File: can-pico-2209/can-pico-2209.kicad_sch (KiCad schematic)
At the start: 13 parts, among them J1 MERG 12v CBUS, J2 Adafruit CAN Pal, J3 DEBUG, J4 UART0, J5 Pico LHS, J6 Pico RHS, SW1 RESET, U1 LM7805_TO220

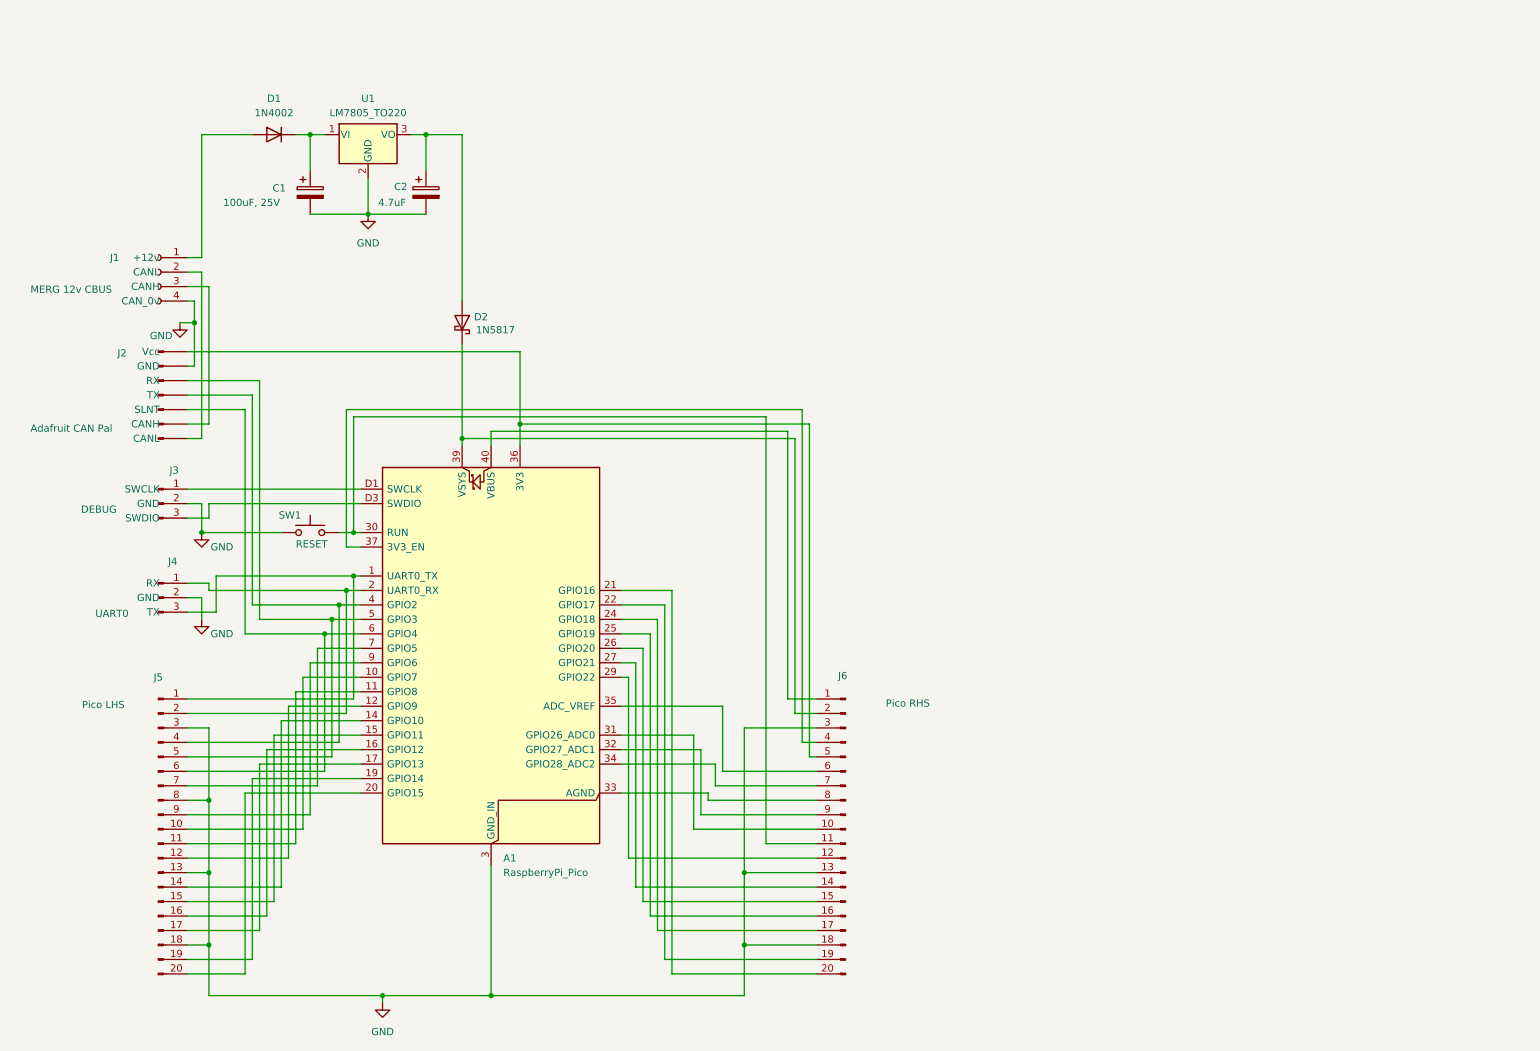
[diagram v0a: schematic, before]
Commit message: now has 2209 module wired in
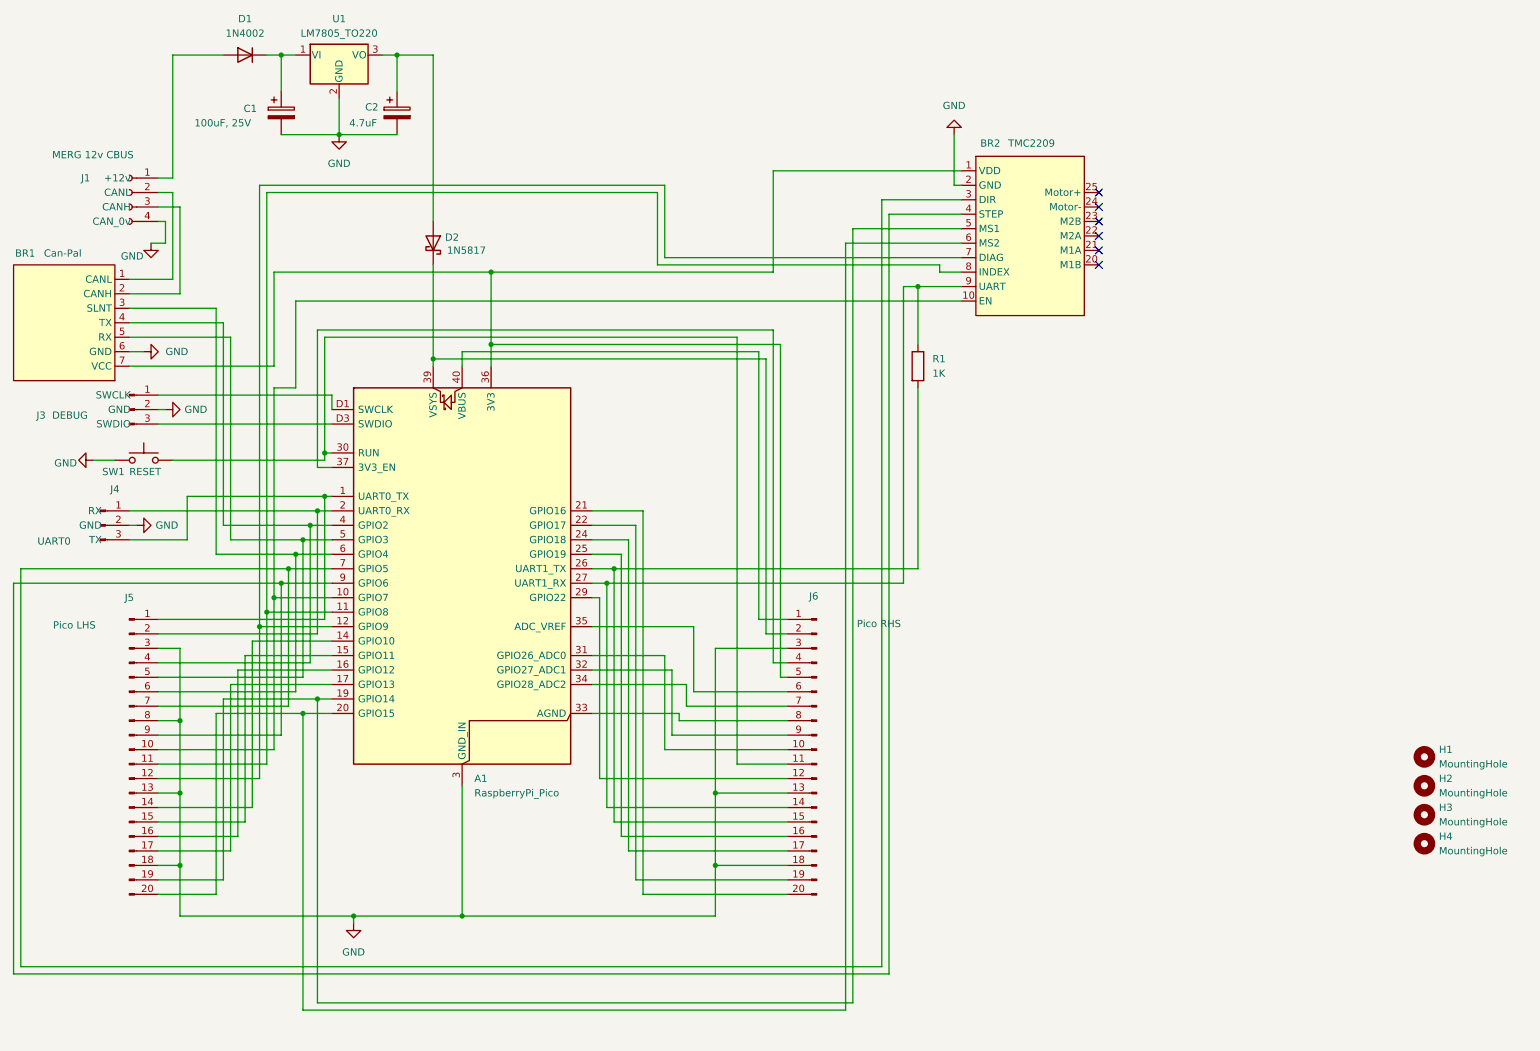
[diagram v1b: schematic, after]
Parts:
- removed J2: Adafruit CAN Pal, Connector_PinHeader_2.54mm:PinHeader_1x07_P2.54mm_Vertical, symbol Connector:Conn_01x07_Pin
- added BR1: Can-Pal, Adafruit:CAN-Pal, symbol Adafruit:CAN-Pal
- added BR2: TMC2209, Adafruit:Adafruit 2209, symbol Adafruit:TMC2209
- added H1, H2, H3, H4: MountingHole, MountingHole:MountingHole_3.2mm_M3, symbol Mechanical:MountingHole
- added R1: 1K, Resistor_THT:R_Axial_DIN0207_L6.3mm_D2.5mm_P10.16mm_Horizontal, symbol Device:R
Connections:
- net GND: now also BR1.6 (GND), BR2.2 (GND)
- net at A1.36 (3V3), J6.5 (Pin_5): now also BR1.7 (VCC), BR2.1 (VDD)
- net at A1.5 (GPIO3), J5.5 (Pin_5): now also BR1.5 (RX)
- net at A1.4 (GPIO2), J5.4 (Pin_4): now also BR1.4 (TX)
- net at A1.6 (GPIO4), J5.6 (Pin_6): now also BR1.3 (SLNT)
- net at J1.3 (CANH): now also BR1.2 (CANH)
- net at J1.2 (CANL): now also BR1.1 (CANL)
- net at A1.10 (GPIO7), J5.10 (Pin_10): now also BR2.10 (EN)
- net at A1.11 (GPIO8), J5.11 (Pin_11): now also BR2.8 (INDEX)
- net at A1.12 (GPIO9), J5.12 (Pin_12): now also BR2.7 (DIAG)
- net at A1.19 (GPIO14), J5.19 (Pin_19): now also BR2.5 (MS1)
- net at A1.20 (GPIO15), J5.20 (Pin_20): now also BR2.6 (MS2)
- net at A1.7 (GPIO5), J5.7 (Pin_7): now also BR2.3 (DIR)
- net at A1.9 (GPIO6), J5.9 (Pin_9): now also BR2.4 (STEP)
- net at A1.27 (GPIO21), J6.14 (Pin_14): now also BR2.9 (UART), R1.1
- net at A1.26 (GPIO20), J6.15 (Pin_15): now also R1.2
- no-connect marks 0 -> 6
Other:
- title: 12v Pico + CAN -> CAN Pico 2209
- moved on the sheet: A1, C1, C2, D1, D2, J1, J3, J4, J5, J6, SW1, U1
